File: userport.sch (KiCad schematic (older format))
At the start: 24 parts, among them CN10 USERPORT, U122 74LS654, U21 74LS04, U22 MOS_6529, U23 MOS_6551_ACIA, Y2 1.8432M

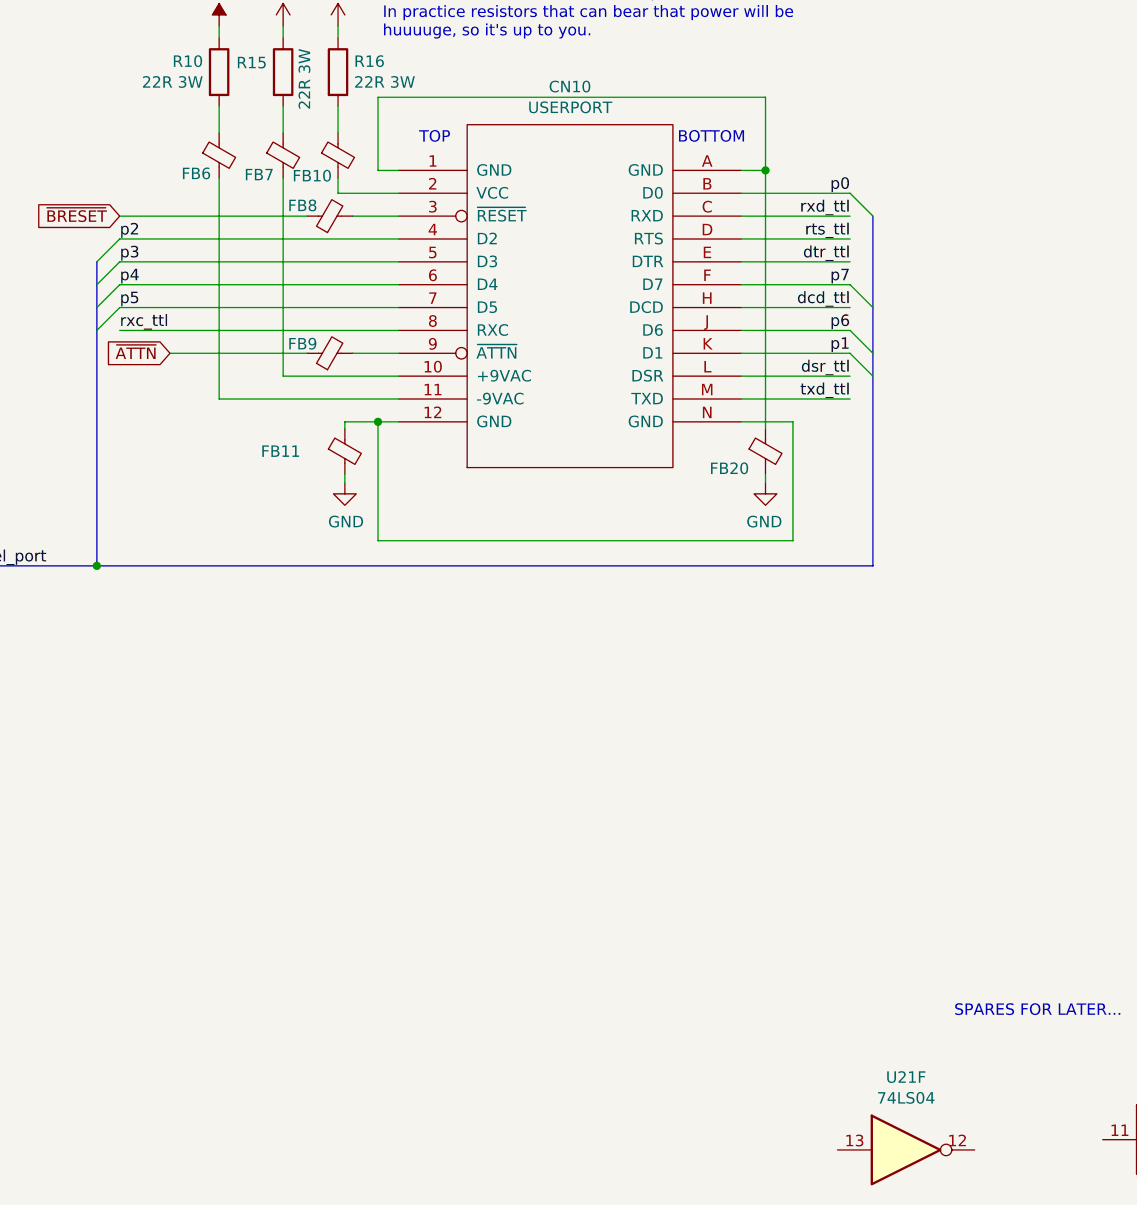
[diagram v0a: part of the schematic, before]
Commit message: Add SID schematics
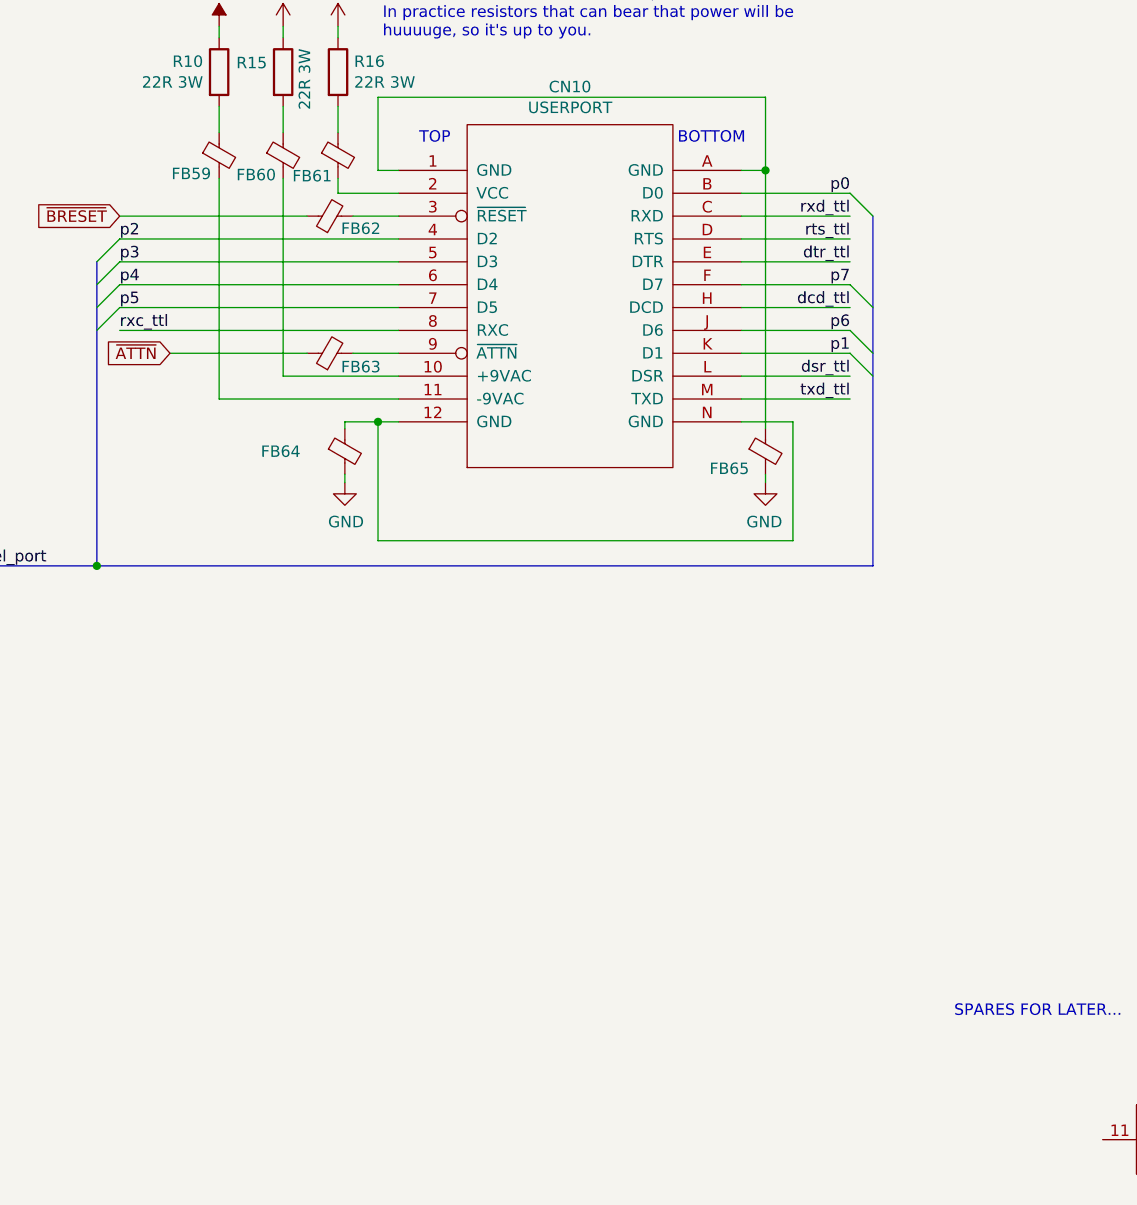
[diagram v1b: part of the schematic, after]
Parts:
- removed unit 6 of U21
- renumbered FB6 to FB59, FB7 to FB60, FB10 to FB61, FB8 to FB62, FB9 to FB63, FB11 to FB64, FB20 to FB65
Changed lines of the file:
@@
 $Descr A3 16535 11693
 encoding utf-8
-Sheet 13 13
-Title "16up"
+Sheet 13 14
+Title "LittleSixteen"
 Date "2023-02-14"
-Rev "2git"
+Rev "3git"
 Comp "SukkoPera"
 Comment1 "Licensed under CC BY-NC-SA 4.0"
@@
 $Comp
 L 74xx:74LS04 U21
-U 6 1 640B6670
-P 9910 10815
-F 0 "U21" H 9910 11132 50  0000 C CNN
-F 1 "74LS04" H 9910 11041 50  0000 C CNN
-F 2 "" H 9910 10815 50  0001 C CNN
-F 3 "http://www.ti.com/lit/gpn/sn74LS04" H 9910 10815 50  0001 C CNN
-	6    9910 10815
-	1    0    0    -1
-$EndComp
-$Comp
-L 74xx:74LS04 U21
 U 7 1 640B7953
 P 2975 10020
@@
 P 7390 6730
 AR Path="/5ECB474B/647718B2" Ref="FB?"  Part="1"
-AR Path="/63EAD078/647718B2" Ref="FB8"  Part="1"
-F 0 "FB8" V 7435 6850 50  0000 C CNN
+AR Path="/63EAD078/647718B2" Ref="FB62"  Part="1"
+F 0 "FB62" V 7335 6595 50  0000 C CNN
 F 1 "Ferrite_Bead_Small" H 7490 6685 50  0001 L CNN
 F 2 "LittleSixteen:Ferrite" V 7320 6730 50  0001 C CNN
@@
 P 7185 6465
 AR Path="/5ECB474B/6477BD12" Ref="FB?"  Part="1"
-AR Path="/63EAD078/6477BD12" Ref="FB7"  Part="1"
-F 0 "FB7" H 7015 6380 50  0000 L CNN
+AR Path="/63EAD078/6477BD12" Ref="FB60"  Part="1"
+F 0 "FB60" H 6980 6380 50  0000 L CNN
 F 1 "Ferrite_Bead_Small" H 7285 6420 50  0001 L CNN
 F 2 "LittleSixteen:Ferrite" V 7115 6465 50  0001 C CNN
@@
 P 7455 7760
 AR Path="/5ECB474B/64790452" Ref="FB?"  Part="1"
-AR Path="/63EAD078/64790452" Ref="FB11"  Part="1"
-F 0 "FB11" H 7261 7760 50  0000 R CNN
+AR Path="/63EAD078/64790452" Ref="FB64"  Part="1"
+F 0 "FB64" H 7261 7760 50  0000 R CNN
 F 1 "Ferrite_Bead_Small" H 7555 7715 50  0001 L CNN
 F 2 "LittleSixteen:Ferrite" V 7385 7760 50  0001 C CNN
@@
 P 9295 7760
 AR Path="/5ECB474B/647AEC6A" Ref="FB?"  Part="1"
-AR Path="/63EAD078/647AEC6A" Ref="FB20"  Part="1"
-F 0 "FB20" H 9050 7685 50  0000 L CNN
+AR Path="/63EAD078/647AEC6A" Ref="FB65"  Part="1"
+F 0 "FB65" H 9050 7685 50  0000 L CNN
 F 1 "Ferrite_Bead_Small" H 9395 7715 50  0001 L CNN
 F 2 "LittleSixteen:Ferrite" V 9225 7760 50  0001 C CNN
@@
 P 7425 6465
 AR Path="/5ECB474B/647B8E58" Ref="FB?"  Part="1"
-AR Path="/63EAD078/647B8E58" Ref="FB10"  Part="1"
-F 0 "FB10" H 7225 6375 50  0000 L CNN
+AR Path="/63EAD078/647B8E58" Ref="FB61"  Part="1"
+F 0 "FB61" H 7225 6375 50  0000 L CNN
 F 1 "Ferrite_Bead_Small" H 7525 6420 50  0001 L CNN
 F 2 "LittleSixteen:Ferrite" V 7355 6465 50  0001 C CNN
@@
 P 7390 7330
 AR Path="/5ECB474B/6479A5EF" Ref="FB?"  Part="1"
-AR Path="/63EAD078/6479A5EF" Ref="FB9"  Part="1"
-F 0 "FB9" V 7430 7450 50  0000 C CNN
+AR Path="/63EAD078/6479A5EF" Ref="FB63"  Part="1"
+F 0 "FB63" V 7330 7195 50  0000 C CNN
 F 1 "Ferrite_Bead_Small" H 7490 7285 50  0001 L CNN
 F 2 "LittleSixteen:Ferrite" V 7320 7330 50  0001 C CNN
@@
 P 6905 6465
 AR Path="/5ECB474B/647EB007" Ref="FB?"  Part="1"
-AR Path="/63EAD078/647EB007" Ref="FB6"  Part="1"
-F 0 "FB6" H 6870 6385 50  0000 R CNN
+AR Path="/63EAD078/647EB007" Ref="FB59"  Part="1"
+F 0 "FB59" H 6870 6385 50  0000 R CNN
 F 1 "Ferrite_Bead_Small" H 7005 6420 50  0001 L CNN
 F 2 "LittleSixteen:Ferrite" V 6835 6465 50  0001 C CNN

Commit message: Place components on board
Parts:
- removed C43: 100n, Capacitor_THT:C_Disc_D7.0mm_W2.5mm_P5.00mm, symbol Device:C
- added C61: 100n, Capacitor_THT:C_Disc_D8.0mm_W2.5mm_P5.00mm, symbol Device:C
- added U28: GAL16V8, Package_DIP:DIP-20_W7.62mm_Socket_LongPads, symbol Logic_Programmable:GAL16V8
- C42, C44: footprint Capacitor_THT:C_Disc_D7.0mm_W2.5mm_P5.00mm -> Capacitor_THT:C_Disc_D8.0mm_W2.5mm_P5.00mm
- C43: renamed from C2; footprint Capacitor_THT:C_Disc_D7.0mm_W2.5mm_P5.00mm -> Capacitor_THT:C_Disc_D8.0mm_W2.5mm_P5.00mm
- U21: footprint (none) -> Package_DIP:DIP-14_W7.62mm_Socket_LongPads
- renumbered R10 to R38, R15 to R39, R16 to R40, R17 to R41, R18 to R42
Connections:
- net GND: now also C61.2, U28.10 (GND)
- net PHI2: now also U28.13 (IO7)
- net R_~W: now also U28.12 (IO8)
- net VCC: now also C61.1, U28.20 (VCC)
- net a0: now also U28.11 (I10/~OE~)
- net a1: now also U28.9 (I9)
- net cba: now also U28.15 (IO5)
- net gab: now also U28.14 (IO6)
- net ~ATTN: now also FB63.2; no longer FB63.1
- net ~BRESET: now also FB62.2; no longer FB62.1
- net at CN10.10 (+9VAC): now also FB60.1; no longer FB60.2
- net at CN10.11 (-9VAC): now also FB59.1; no longer FB59.2
- net at CN10.2 (VCC): now also FB61.1; no longer FB61.2
- net at CN10.3 (~RESET): now also FB62.1; no longer FB62.2
- net at CN10.9 (~ATTN): now also FB63.1; no longer FB63.2
- net at R39.2: now also FB60.2; no longer FB60.1
- net at R40.2: now also FB61.2; no longer FB61.1
- net at R38.2: now also FB59.2; no longer FB59.1
- net q+: now reaches U23.6 (XTLI), Y2.2
- net q-: now reaches U23.7 (XTLO), Y2.1
- new net A15_10_HIGH: U28.19 (IO1)
- new net a2: U28.8 (I8)
- new net a3: U28.7 (I7)
- new net a4: U28.6 (I6)
- new net a5: U28.5 (I5)
- new net a6: U28.4 (I4)
- new net a7: U28.3 (I3)
- new net a8: U28.2 (I2)
- new net a9: U28.1 (I1/CLK)
- new net ramreg_wcs: U28.16 (IO4)
- new net ~ramreg_rcs: U28.17 (I03)
- new net ~userport_cs: U28.18 (IO2)
- no-connect marks 0 -> 2
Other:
- note added: "$FD10 ONLY!"
- note added: "CHIP-SELECT\nGENERATION"

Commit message: Routing in progress
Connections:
- net dtr_ttl: now also U21.4; no longer U21.2
- net rts_ttl: now also U21.2; no longer U21.4
- net ~dtr_ttl: now also U21.3; no longer U21.1
- net ~rts_ttl: now also U21.1; no longer U21.3
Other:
- moved on the sheet: U21A, U21B
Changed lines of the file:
@@
 L 74xx:74LS04 U21
 U 1 1 640B17BF
-P 8690 2340
-F 0 "U21" H 8690 2657 50  0000 C CNN
-F 1 "74LS04" H 8690 2566 50  0000 C CNN
-F 2 "Package_DIP:DIP-14_W7.62mm_Socket_LongPads" H 8690 2340 50  0001 C CNN
-F 3 "http://www.ti.com/lit/gpn/sn74LS04" H 8690 2340 50  0001 C CNN
-	1    8690 2340
+P 8690 2745
+F 0 "U21" H 8690 3062 50  0000 C CNN
+F 1 "74LS04" H 8690 2971 50  0000 C CNN
+F 2 "Package_DIP:DIP-14_W7.62mm_Socket_LongPads" H 8690 2745 50  0001 C CNN
+F 3 "http://www.ti.com/lit/gpn/sn74LS04" H 8690 2745 50  0001 C CNN
+	1    8690 2745
 	1    0    0    -1
 $EndComp
@@
 L 74xx:74LS04 U21
 U 2 1 640B2561
-P 8690 2745
-F 0 "U21" H 8690 2970 50  0000 C CNN
-F 1 "74LS04" H 8690 2971 50  0001 C CNN
-F 2 "Package_DIP:DIP-14_W7.62mm_Socket_LongPads" H 8690 2745 50  0001 C CNN
-F 3 "http://www.ti.com/lit/gpn/sn74LS04" H 8690 2745 50  0001 C CNN
-	2    8690 2745
+P 8690 2340
+F 0 "U21" H 8690 2565 50  0000 C CNN
+F 1 "74LS04" H 8690 2566 50  0001 C CNN
+F 2 "Package_DIP:DIP-14_W7.62mm_Socket_LongPads" H 8690 2340 50  0001 C CNN
+F 3 "http://www.ti.com/lit/gpn/sn74LS04" H 8690 2340 50  0001 C CNN
+	2    8690 2340
 	1    0    0    -1
 $EndComp

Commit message: Well yeah maybe
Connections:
- no-connect marks 2 -> 3
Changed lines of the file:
@@
 Text Label 3245 2925 0    50   ~ 0
 q-
+NoConn ~ 3795 6395
 Wire Bus Line
 	9765 6730 9765 8260

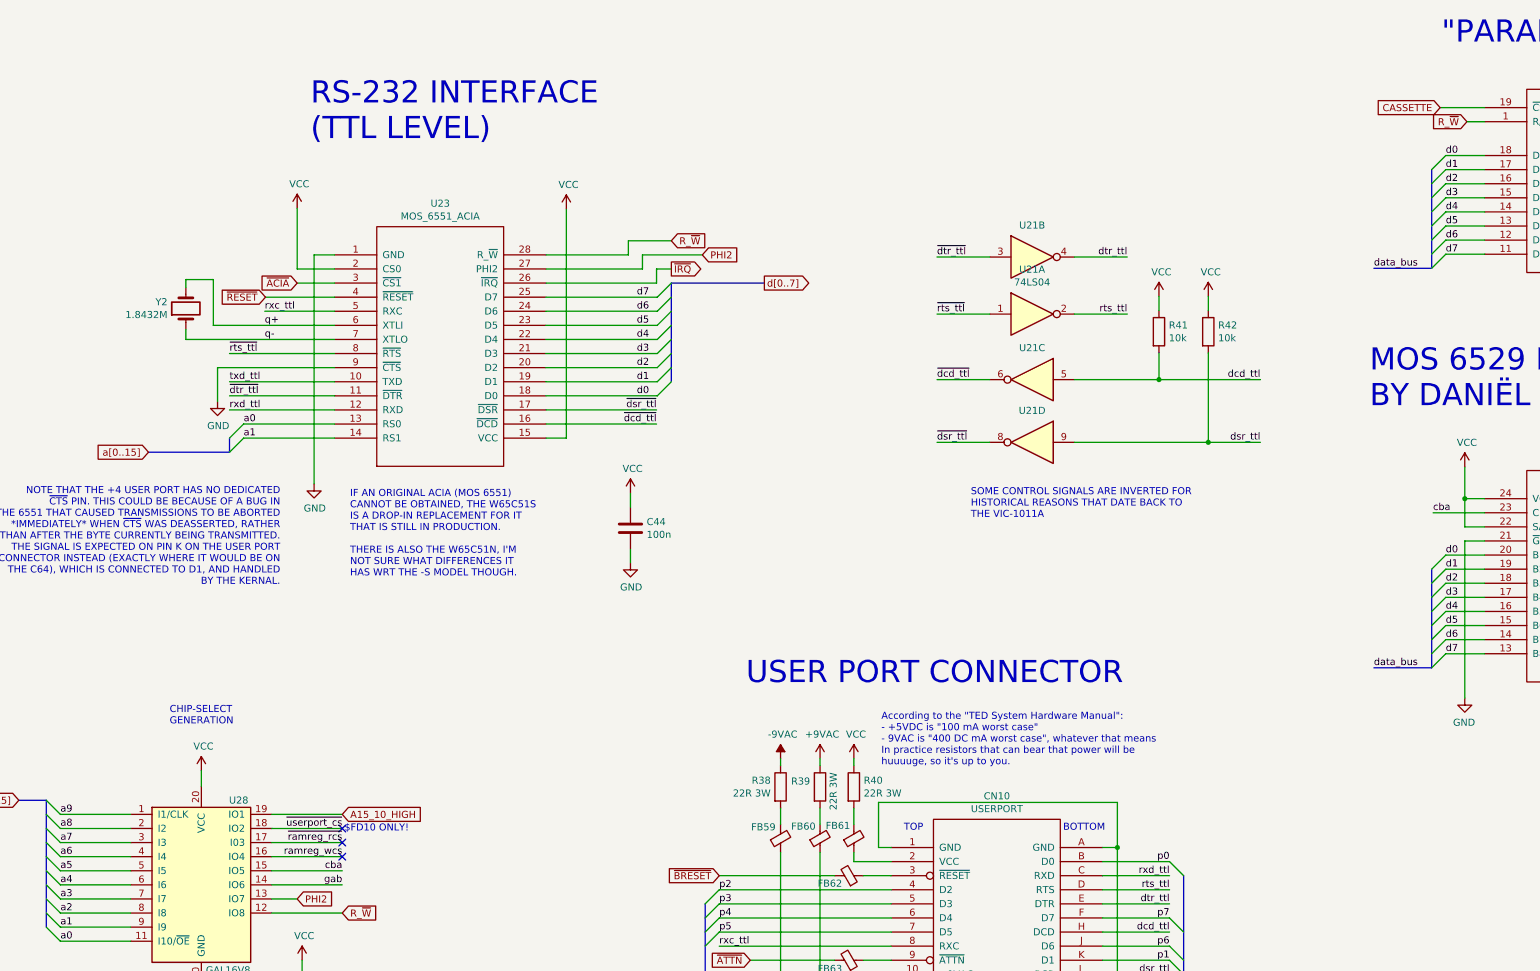
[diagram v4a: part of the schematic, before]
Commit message: Add 512kB RAM expansions, Hannes-style
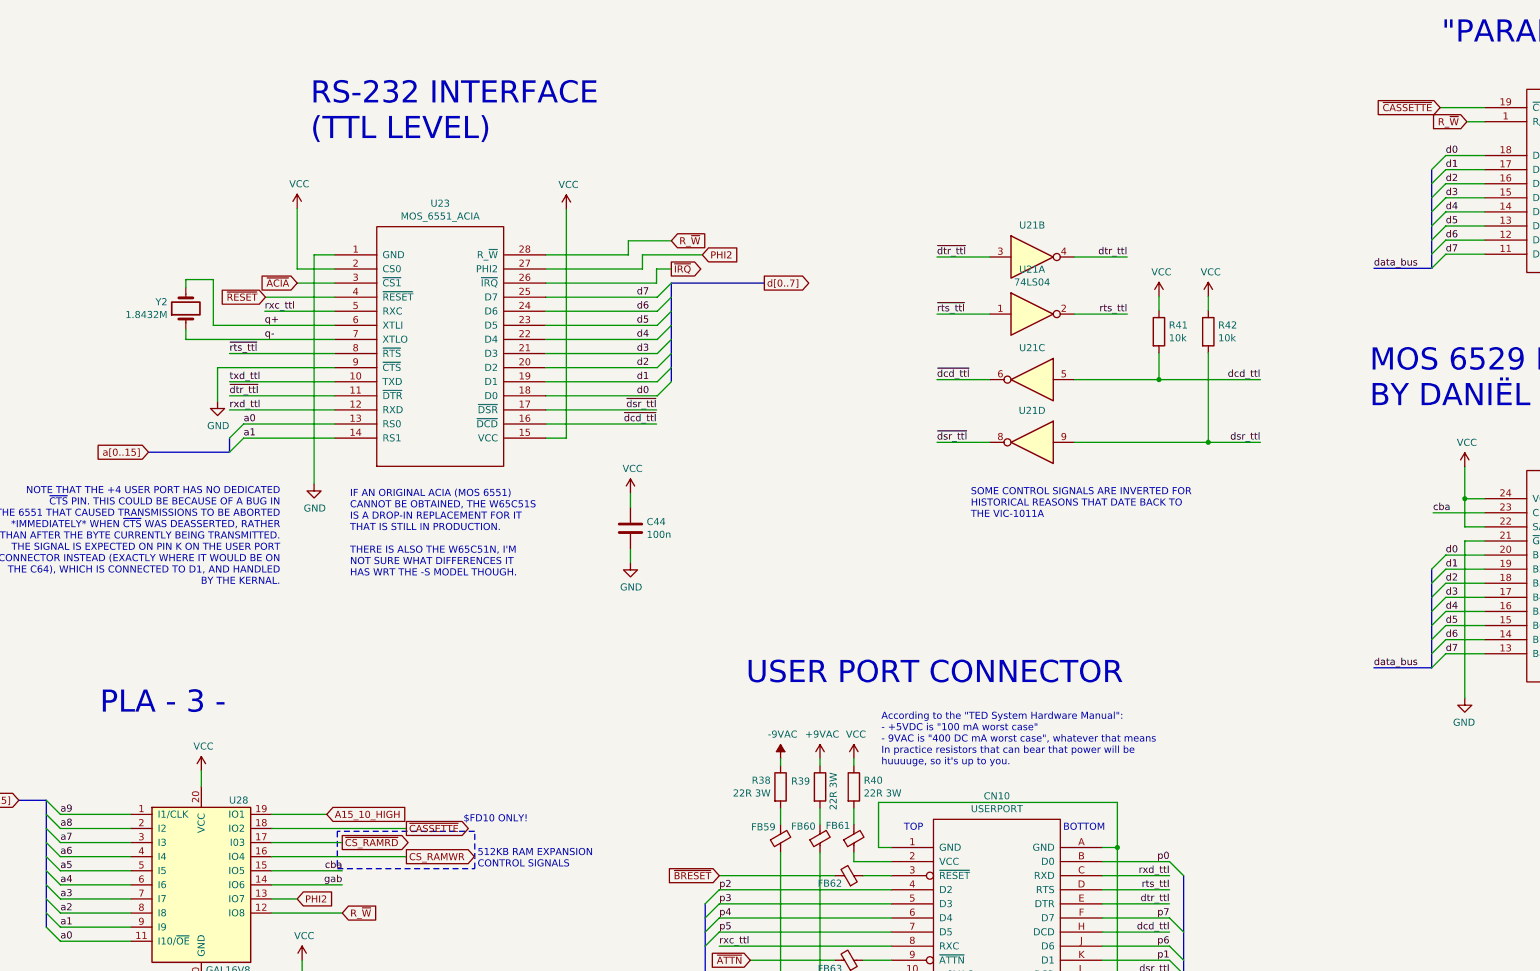
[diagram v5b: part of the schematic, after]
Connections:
- net ~userport_cs is gone; now on net ~CASSETTE: U28.18 (IO2)
- net CASSETTE renamed ~CASSETTE
- net ramreg_wcs renamed CS_RAMWR
- net ~ramreg_rcs renamed ~CS_RAMRD
- no-connect marks 3 -> 0
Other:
- note added: "512KB RAM EXPANSION\nCONTROL SIGNALS"
- note added: "PLA - 3 -"
- note removed: "CHIP-SELECT\nGENERATION"
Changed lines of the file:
@@
 	7290 6730 6470 6730
 Text GLabel 11585 1280 0    50   Input ~ 0
-CASSETTE
+~CASSETTE
 Text GLabel 11775 1380 0    50   Input ~ 0
 R_~W
@@
 	3795 6695 3295 6695
 Wire Wire Line
-	3795 6395 3295 6395
-Wire Wire Line
-	3795 6295 3295 6295
+	4250 6395 3295 6395
+Wire Wire Line
+	3685 6295 3295 6295
 Wire Wire Line
 	2295 7095 1795 7095
@@
 Wire Wire Line
 	2295 6295 1795 6295
-Text Notes 3810 6425 0    50   ~ 0
+Text Notes 4655 6360 0    50   ~ 0
 $FD10 ONLY!
 Entry Wire Line
@@
 Entry Wire Line
 	1695 6195 1795 6295
-Text Notes 2570 5665 0    50   ~ 0
-CHIP-SELECT\nGENERATION
 $Comp
 L Device:C C?
@@
 Wire Bus Line
 	1500 6195 1695 6195
-Text GLabel 3795 6295 2    50   Input ~ 0
+Text GLabel 3685 6295 2    50   Input ~ 0
 A15_10_HIGH
 Wire Wire Line
@@
 R_~W
 Wire Wire Line
-	3795 6595 3295 6595
+	4250 6595 3295 6595
 Text Label 3795 6795 2    50   ~ 0
 gab
@@
 Text Label 1795 7195 0    50   ~ 0
 a0
-Text Label 3795 6395 2    50   ~ 0
-~userport_cs
-Text Label 3795 6495 2    50   ~ 0
-~ramreg_rcs
-Text Label 3795 6595 2    50   ~ 0
-ramreg_wcs
-NoConn ~ 3795 6495
-NoConn ~ 3795 6595
 Text Label 3245 2825 0    50   ~ 0
 q+
 Text Label 3245 2925 0    50   ~ 0
 q-
-NoConn ~ 3795 6395
+Text Notes 2075 5595 0    157  ~ 0
+PLA - 3 -
+Text GLabel 3795 6495 2    50   Output ~ 0
+~CS_RAMRD
+Text GLabel 4250 6595 2    50   Output ~ 0
+CS_RAMWR
+Text GLabel 4250 6395 2    50   Output ~ 0
+~CASSETTE
+Wire Notes Line
+	3760 6415 3760 6680
+Wire Notes Line
+	3760 6680 4735 6680
+Wire Notes Line
+	4735 6680 4735 6415
+Wire Notes Line
+	4735 6415 3760 6415
+Text Notes 4755 6680 0    50   ~ 0
+512KB RAM EXPANSION\nCONTROL SIGNALS
 Wire Bus Line
 	9765 6730 9765 8260
